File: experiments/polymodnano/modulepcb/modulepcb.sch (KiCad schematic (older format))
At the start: 23 parts

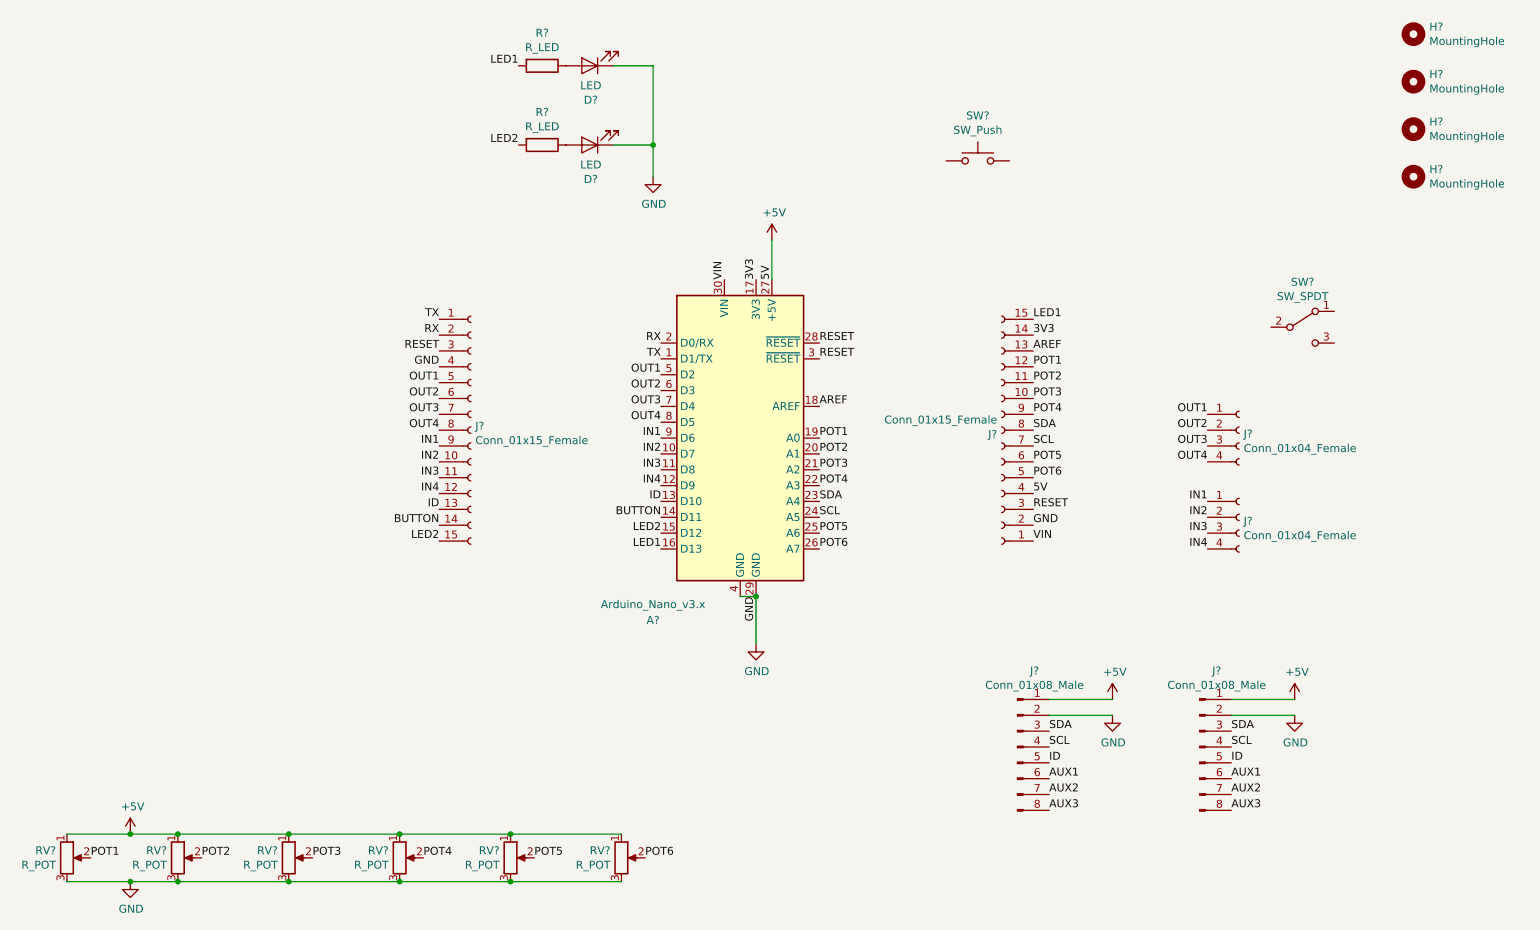
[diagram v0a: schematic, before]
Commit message: created 8hp test module
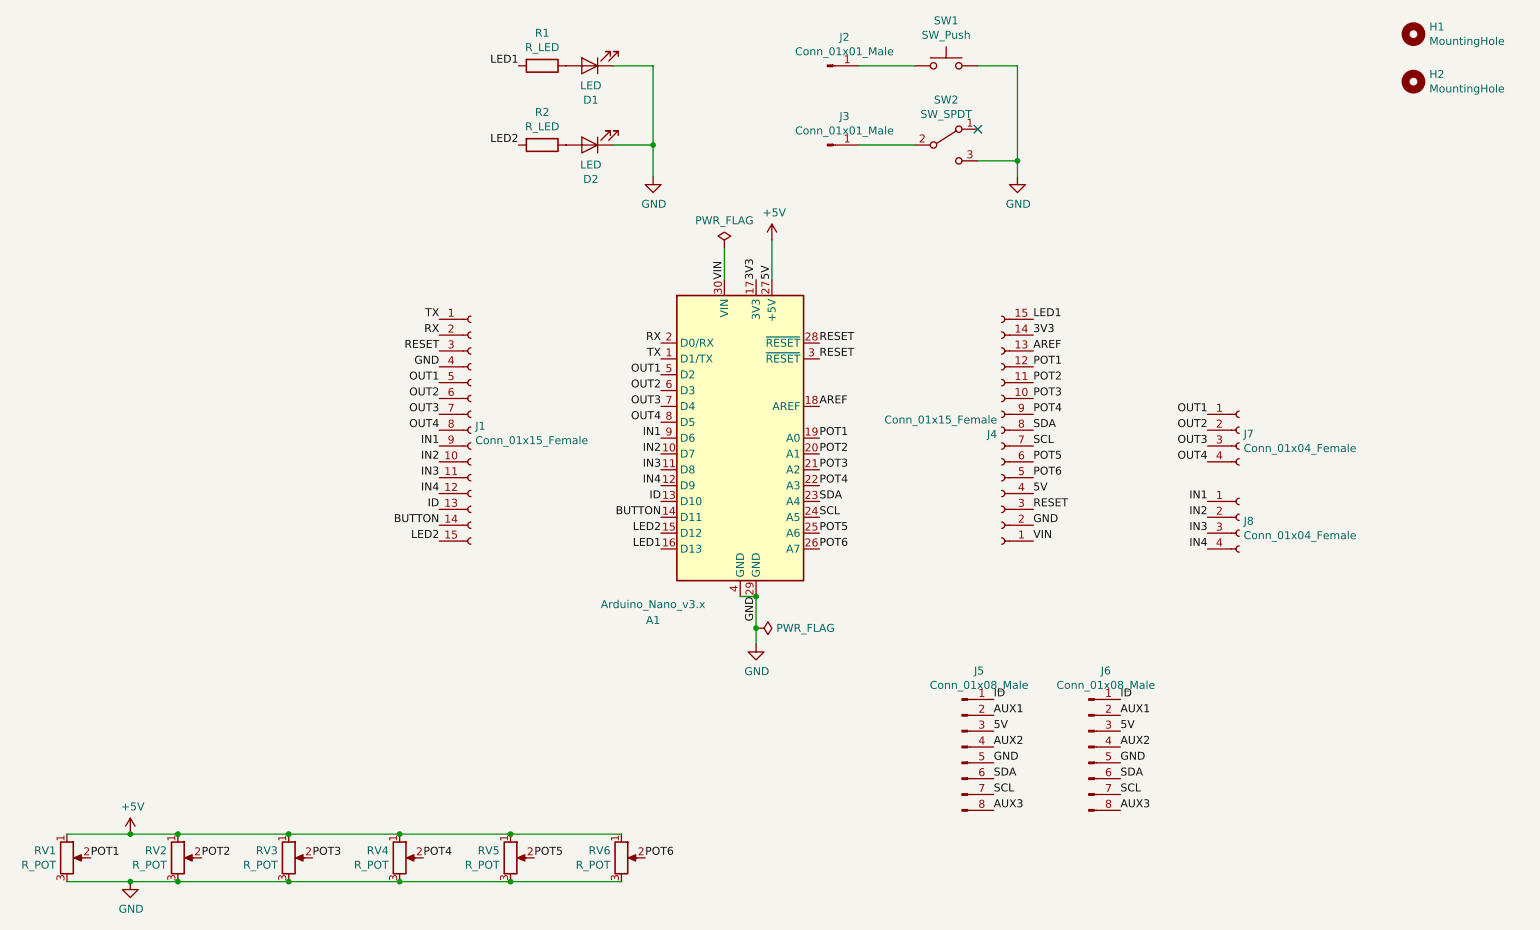
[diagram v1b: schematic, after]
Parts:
- removed H? (x2): MountingHole, symbol Mechanical:MountingHole
- removed J?: Conn_01x08_Male, symbol Connector:Conn_01x08_Male
- added J2, J3: Conn_01x01_Male, Connector_PinHeader_2.54mm:PinHeader_1x01_P2.54mm_Vertical, symbol Connector:Conn_01x01_Male
- added J6: Conn_01x08_Male, Connector_PinHeader_2.54mm:PinHeader_1x08_P2.54mm_Vertical, symbol Connector:Conn_01x08_Male
- D1, D2: renamed from D?; footprint (none) -> LED_THT:LED_D5.0mm
- H1, H2: renamed from H?; footprint (none) -> MountingHole:MountingHole_3.2mm_M3
- J1, J4: renamed from J?; footprint (none) -> Connector_PinHeader_2.54mm:PinHeader_1x15_P2.54mm_Vertical
- J5: renamed from J?; footprint (none) -> Connector_PinHeader_2.54mm:PinHeader_1x08_P2.54mm_Vertical
- J7, J8: renamed from J?; footprint (none) -> Connector_PinSocket_2.54mm:PinSocket_1x04_P2.54mm_Vertical
- R1, R2: renamed from R?; footprint (none) -> Resistor_THT:R_Axial_DIN0204_L3.6mm_D1.6mm_P7.62mm_Horizontal
- RV1, RV2, RV3, RV4, RV5, RV6: renamed from RV?; footprint (none) -> drumkidcustom:Potentiometer_Alps_RK09K_Single_Vertical
- SW1: renamed from SW?; footprint (none) -> Button_Switch_THT:SW_PUSH-12mm_Wuerth-430476085716
- SW2: renamed from SW?; footprint (none) -> drumkidcustom:EG1206
- gave numbers to parts that had none: 1
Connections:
- net +5V: now also J5.3 (Pin_3), J6.3 (Pin_3); no longer J5.1 (Pin_1)
- net AUX1: now also J5.2 (Pin_2), J6.2 (Pin_2); no longer J5.6 (Pin_6)
- net AUX2: now also J5.4 (Pin_4), J6.4 (Pin_4); no longer J5.7 (Pin_7)
- net AUX3: now also J6.8 (Pin_8)
- net GND: now also J5.5 (Pin_5), SW1.2, SW2.3 (C), J6.5 (Pin_5); no longer J5.2 (Pin_2)
- net ID: now also J5.1 (Pin_1), J6.1 (Pin_1); no longer J5.5 (Pin_5)
- net SCL: now also J5.7 (Pin_7), J6.7 (Pin_7); no longer J5.4 (Pin_4)
- net SDA: now also J5.6 (Pin_6), J6.6 (Pin_6); no longer J5.3 (Pin_3)
- net at SW1.1: now also J2.1 (Pin_1)
- net at SW2.2 (B): now also J3.1 (Pin_1)
- no-connect marks 0 -> 1
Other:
- moved on the sheet: J5, SW1, SW2
